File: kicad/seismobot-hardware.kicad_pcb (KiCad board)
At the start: 2 copper layers, 110 x 100 mm, 92 parts, among them J1 Screw_Terminal_01x02, J2 Raspberry_Pi_2_3, U1 OPA2156xD, U2 OPA2156xD, U3 LTC6011, U4 ref-6, U5 ref-8, U6 OPA2156xD, U7 OPA2156xD, U8 MAX11200, U9 ATSAMD09C13A-SS, X1 SG-5032CAN, Y1 32768 Hz

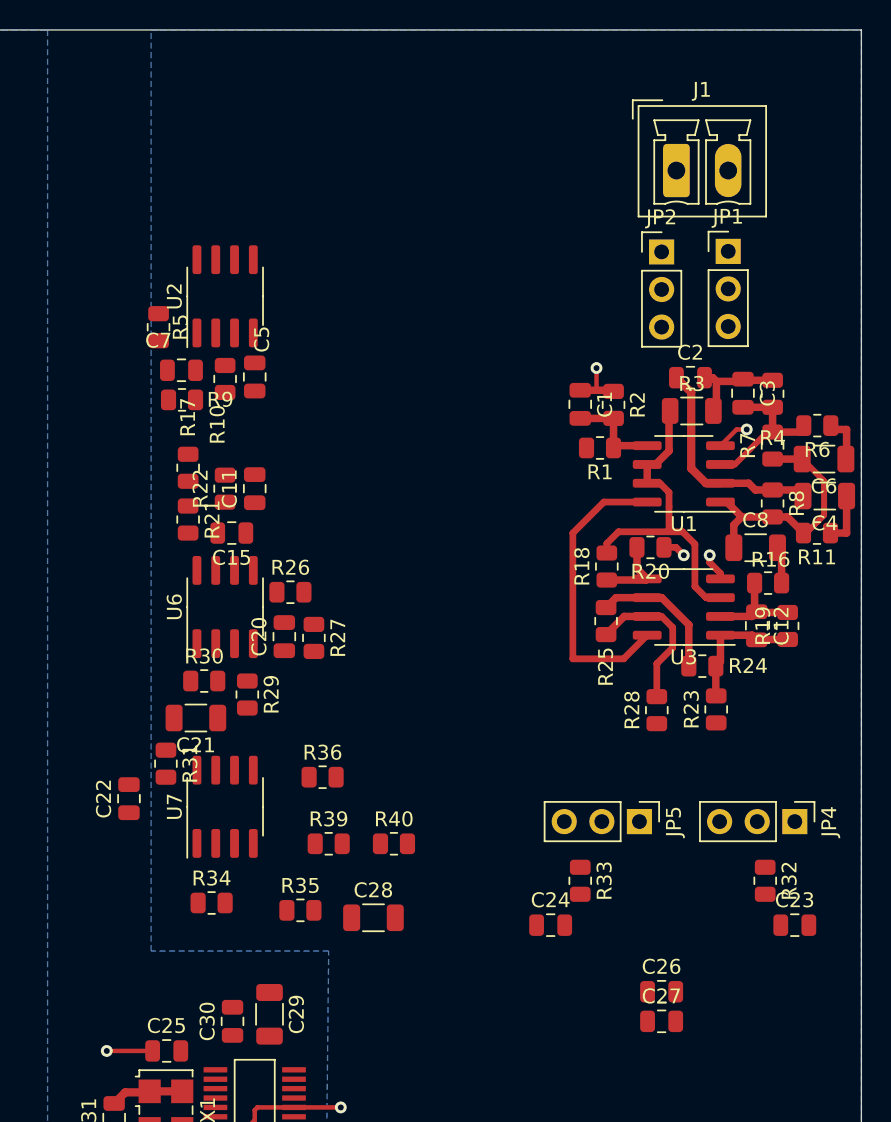
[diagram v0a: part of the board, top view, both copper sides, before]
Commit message: add v2 signal path routing
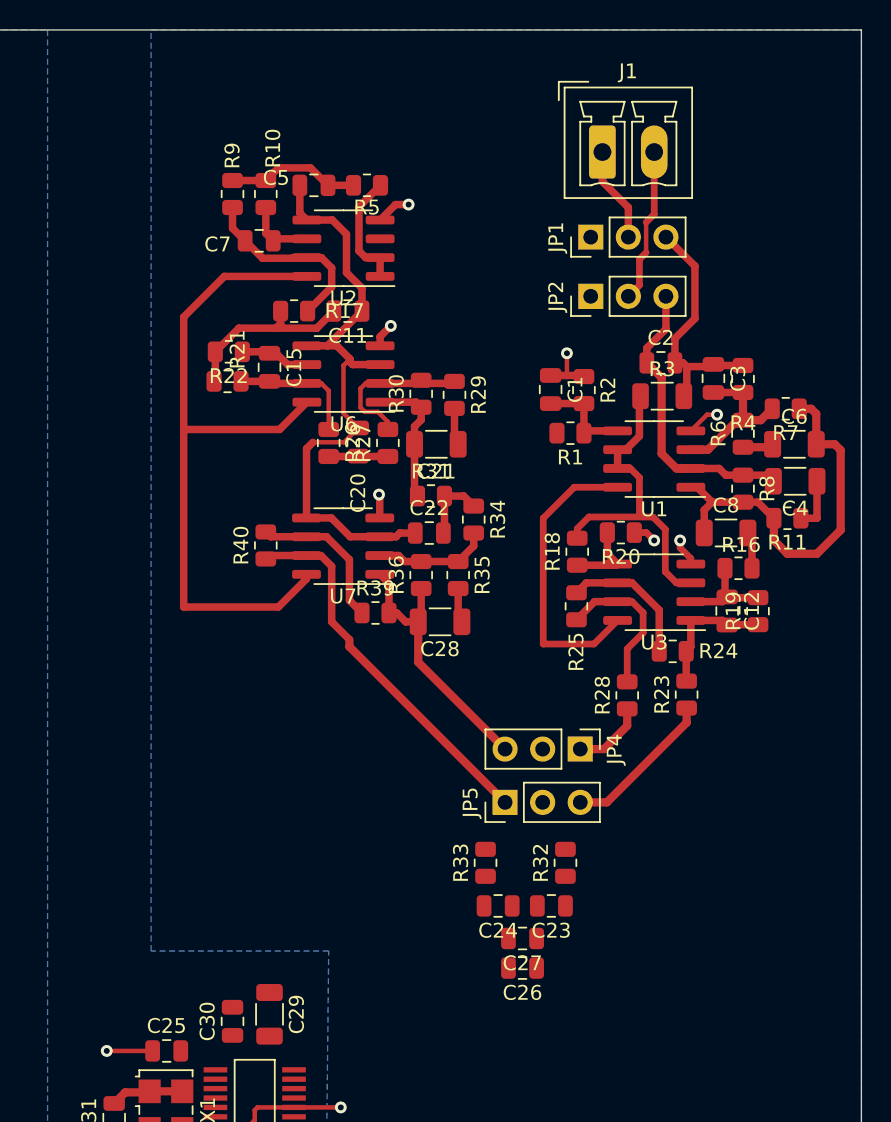
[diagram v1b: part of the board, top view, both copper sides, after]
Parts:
- moved R34 31.4 mm to (163.8, 123.1), turned to 270 degrees
- moved C22 27.1 mm to (160.8, 124.0), turned to 0 degrees
- moved R31 25.5 mm to (160.9, 121.5), turned to 0 degrees
- moved R35 25.0 mm to (162.8, 126.8), turned to 270 degrees
- moved C21 24.6 mm to (161.3, 118.0)
- moved R29 24.6 mm to (162.5, 114.7)
- moved R30 24.3 mm to (160.2, 114.6), turned to 90 degrees
- moved R40 21.9 mm to (149.8, 124.8), turned to 90 degrees
- moved C28 20.5 mm to (161.5, 130.0), turned to 180 degrees
- moved U7 19.3 mm to (155.0, 124.9), turned to 180 degrees
- moved U6 17.7 mm to (155.0, 113.2), turned to 180 degrees
- moved R5 17.0 mm to (156.6, 100.5), turned to 0 degrees
- moved C23 16.5 mm to (169.1, 149.2), turned to 180 degrees
- moved R39 15.9 mm to (157.2, 129.4)
- moved JP4 15.3 mm to (171.0, 138.6)
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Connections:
- JP4 pad 3: Net-(JP4-Pad3) -> OUTb+
- JP5 pad 1: Net-(JP5-Pad1) -> OUTb-
- U2 pad 1: Net-(C7-Pad2) -> Net-(R5-Pad2)
- U2 pad 2: Net-(C7-Pad1) -> Net-(R5-Pad2)
- U2 pad 3: 1.5v -> Gb+
- U2 pad 5: Gb+ -> 1.5v
- U2 pad 6: Net-(R5-Pad2) -> Net-(C7-Pad1)
- U2 pad 7: Net-(R5-Pad2) -> Net-(C7-Pad2)
- U7 pad 1: OUTb- -> OUTb+
- U7 pad 2: Net-(R39-Pad1) -> Net-(R34-Pad2)
- U7 pad 6: Net-(R34-Pad2) -> Net-(R39-Pad1)
- U7 pad 7: OUTb+ -> OUTb-
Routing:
- net +3V3: track 25.0 -> 72.6 mm
- net 1.5v: track 22.3 -> 64.4 mm
- net OUTb-: track 0.00 -> 25.7 mm
- net OUTb+: track 0.00 -> 18.5 mm
- net Net-(C7-Pad2): track 0.00 -> 12.8 mm
- net Net-(C11-Pad2): track 0.00 -> 12.5 mm
- net Net-(R27-Pad2): track 0.00 -> 10.6 mm
- net Net-(J1-Pad2): track 0.00 -> 10.5 mm
- net OUTa-: track 0.00 -> 10.4 mm
- net Net-(R39-Pad1): track 0.00 -> 10.4 mm
- net Ga+: track 6.82 -> 16.7 mm
- net Net-(C6-Pad2): track 17.1 -> 26.6 mm
- net Net-(C21-Pad2): track 0.00 -> 9.19 mm
- net Net-(C5-Pad2): track 0.00 -> 9.02 mm
- net Net-(C15-Pad2): track 0.00 -> 8.80 mm
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
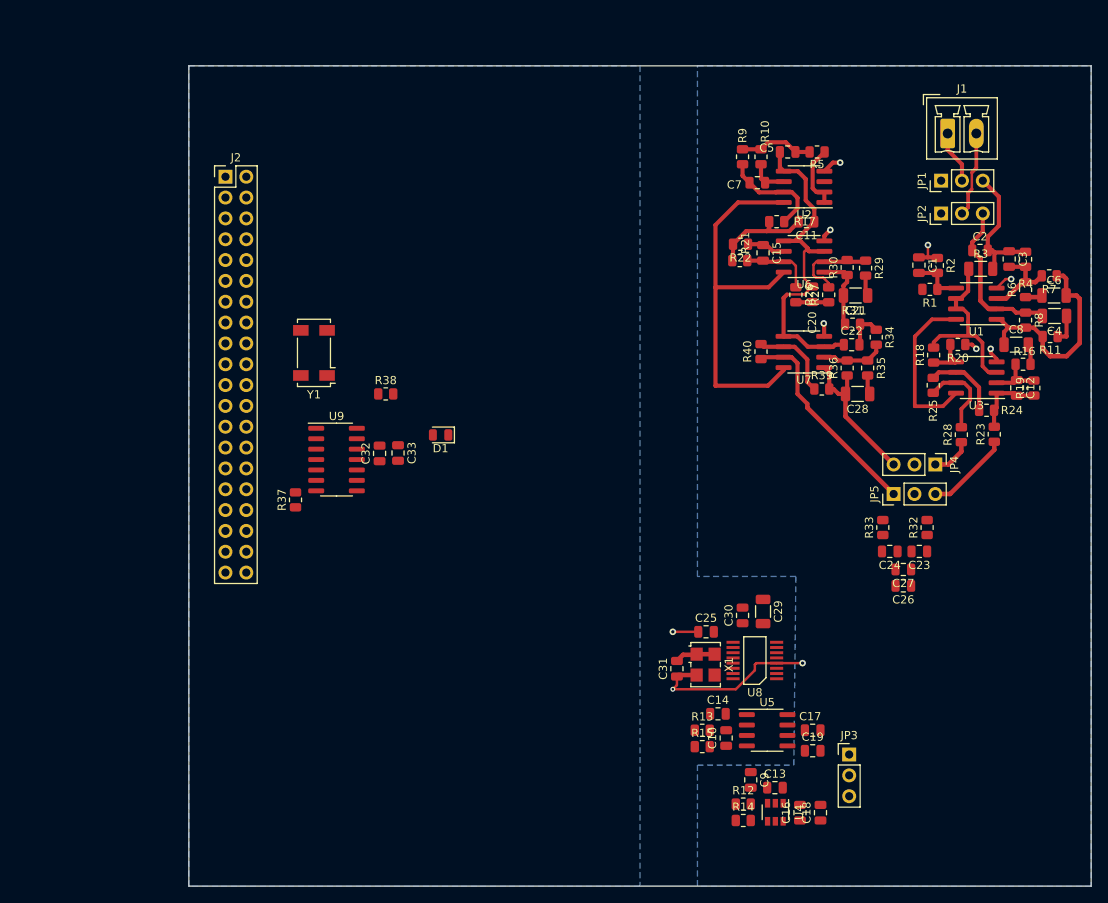
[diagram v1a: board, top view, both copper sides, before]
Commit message: add 3v3 regulator, simplify signal split, add planes
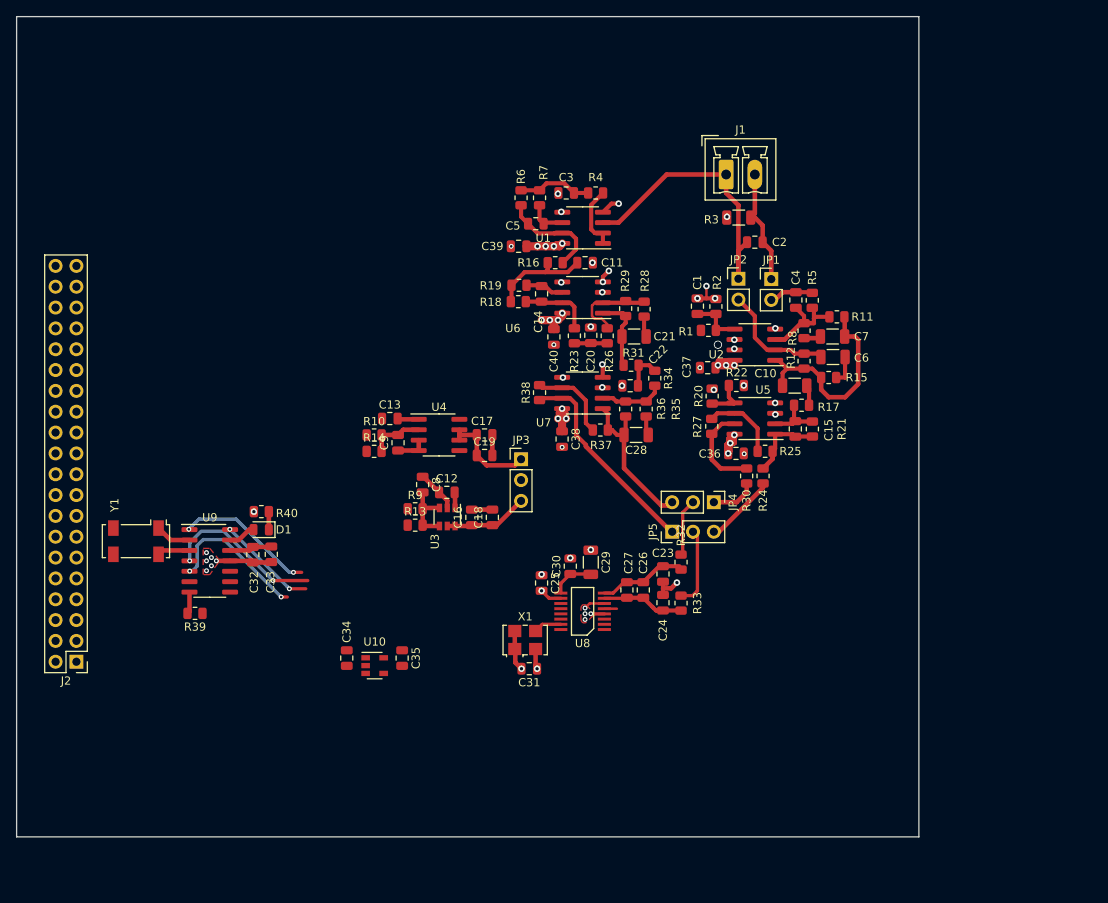
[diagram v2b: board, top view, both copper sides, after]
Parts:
- removed the R38 at (104.0, 130.0)
- removed the U3 at (176.0, 128.0)
- added C34: 1u, Capacitor_SMD:C_0805_2012Metric, F.Cu at (99.2, 162.2)
- added C35: 1u, Capacitor_SMD:C_0805_2012Metric, F.Cu at (106.0, 162.2)
- added C36: 1u, Capacitor_SMD:C_0805_2012Metric, F.Cu at (146.7, 137.2)
- added C37: 1u, Capacitor_SMD:C_0805_2012Metric, F.Cu at (143.2, 126.8)
- added C38: 1u, Capacitor_SMD:C_0805_2012Metric, F.Cu at (125.5, 135.5)
- added C39: 1u, Capacitor_SMD:C_0805_2012Metric, F.Cu at (120.2, 112.0)
- added C40: 1u, Capacitor_SMD:C_0805_2012Metric, F.Cu at (124.5, 123.0)
- added R40: 100, Resistor_SMD:R_0805_2012Metric, F.Cu at (88.8, 144.3)
- added U10: LP5907MFX-3.3, Package_TO_SOT_SMD:SOT-23-5, F.Cu at (102.7, 163.1)
- added U5: LTC6011, Package_SO:SOIC-8_3.9x4.9mm_P1.27mm, F.Cu at (149.0, 133.0)
- JP1, JP2: value Jumper_NC_Dual -> Jumper_2_Open; footprint Connector_PinHeader_2.54mm:PinHeader_1x03_P2.54mm_Vertical -> Connector_PinHeader_2.54mm:PinHeader_1x02_P2.54mm_Vertical
- Y1: value 32768 Hz -> Crystal; footprint Crystal:Crystal_SMD_Abracon_ABS25-4Pin_8.0x3.8mm -> seismobot-hardware:Crystal_SMD_Suntsu_SWS83412D16-4Pin_8.0x3.8mm
- moved J2 61.9 mm to (66.3, 162.7), turned to 180 degrees
- moved C17 53.8 mm to (116.0, 135.0)
- moved C19 53.8 mm to (116.0, 137.5)
- moved C13 53.8 mm to (104.5, 133.0)
- moved C16 53.8 mm to (114.5, 145.1)
- moved C18 53.8 mm to (117.0, 145.1)
- moved C8 53.8 mm to (108.5, 141.1)
- moved C9 53.8 mm to (105.5, 135.9)
- moved JP3 53.8 mm to (120.5, 138.0)
- moved R10 53.8 mm to (102.6, 135.0)
- moved R13 53.8 mm to (107.6, 146.0)
- moved R14 53.8 mm to (102.6, 137.0)
- moved R9 53.8 mm to (107.6, 144.0)
- moved U3 53.8 mm to (111.5, 145.0)
- moved U4 53.8 mm to (110.5, 135.0)
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- renumbered C8 to C10, C13 to C12, C14 to C13, C15 to C14, C12 to C15, C5 to C3, C3 to C4, C7 to C5, C4 to C6, C6 to C7, C9 to C8, C10 to C9, R13 to R10, R7 to R11, R8 to R12, R14 to R13, R15 to R14, R11 to R15, R17 to R16, R16 to R17, R21 to R18, R22 to R19, R18 to R20, R19 to R21, R20 to R22, R26 to R23, R23 to R24, R24 to R25, R27 to R26, R25 to R27, R29 to R28, R30 to R29, R28 to R30, R39 to R37, R40 to R38, R37 to R39, R5 to R4, R4 to R5, R9 to R6, R10 to R7, R6 to R8, R12 to R9, U2 to U1, U1 to U2, U4 to U3, U5 to U4
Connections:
- C2 pad 1: Ga- -> G-
- C2 pad 2: Ga+ -> G+
- C32 pad 2: +3V3 -> VDD
- C33 pad 1: +3V3 -> VDD
- C4 pad 1: Ga+ -> Net-(C4-Pad1)
- C6 pad 2: Ga- -> Net-(C6-Pad2)
- J1 pad 1: Net-(J1-Pad1) -> G-
- J1 pad 2: Net-(J1-Pad2) -> G+
- J2 pad 1: Net-(J2-Pad1) -> VDD
- J2 pad 2: Net-(J2-Pad2) -> +5V
- JP1 pad 1: Gb+ -> G+
- JP1 pad 2: Net-(J1-Pad1) -> Net-(C4-Pad1)
- JP2 pad 1: 1.5v -> G-
- JP2 pad 2: Net-(J1-Pad2) -> Net-(C6-Pad2)
- R12 pad 1: Ga- -> Net-(C6-Pad2)
- R3 pad 2: Ga+ -> G+
- R39 pad 1: +3V3 -> VDD
- R5 pad 2: Ga+ -> Net-(C4-Pad1)
- U1 pad 3: Gb+ -> G-
- U2 pad 2: Ga- -> Net-(C6-Pad2)
- U9 pad 12: +3V3 -> VDD
- U9 pad 2: GND -> Net-(U9-Pad2)
- U9 pad 3: GND -> Net-(U9-Pad3)
- Y1 pad 1: GND -> Net-(U9-Pad2)
- Y1 pad 2: GND -> (no net)
- Y1 pad 4: (no net) -> Net-(U9-Pad3)
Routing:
- net 1.5v: track 64.4 -> 0.00 mm, vias 0 -> 15
- net +3V3: track 72.6 -> 34.7 mm, vias 0 -> 19
- net G-: track 0.00 -> 35.7 mm
- net Ga-: track 19.9 -> 0.00 mm
- net MOSI: track 0.00 -> 19.7 mm, vias 0 -> 2
- net SCK: track 0.00 -> 17.9 mm, vias 0 -> 2
- net CS: track 0.00 -> 17.1 mm, vias 0 -> 2
- net Ga+: track 16.7 -> 0.00 mm
- net Net-(C6-Pad2): track 0.00 -> 15.0 mm
- net G+: track 0.00 -> 14.3 mm
- net MISO: track 0.00 -> 12.3 mm, vias 0 -> 2
- net Net-(C17-Pad1): track 0.00 -> 12.1 mm
- net Net-(C23-Pad1): track 0.00 -> 10.5 mm
- net Net-(J1-Pad2): track 10.5 -> 0.00 mm
- net Net-(JP5-Pad2): track 0.00 -> 10.3 mm
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- added copper zone on In2.Cu, net +3V3
- added copper zone on In2.Cu, net 1.5v
- added copper zone on F.Cu, net GND
- added copper zone on In1.Cu, net GND
- removed copper zone on B.Cu, net GND
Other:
- copper layers 2 -> 4
- board text added: "Josh is thee best"
- board text added: "manny is cool"
